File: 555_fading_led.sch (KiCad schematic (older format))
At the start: 15 parts, among them SW1 power, U1 TLC555, U2 TLC555

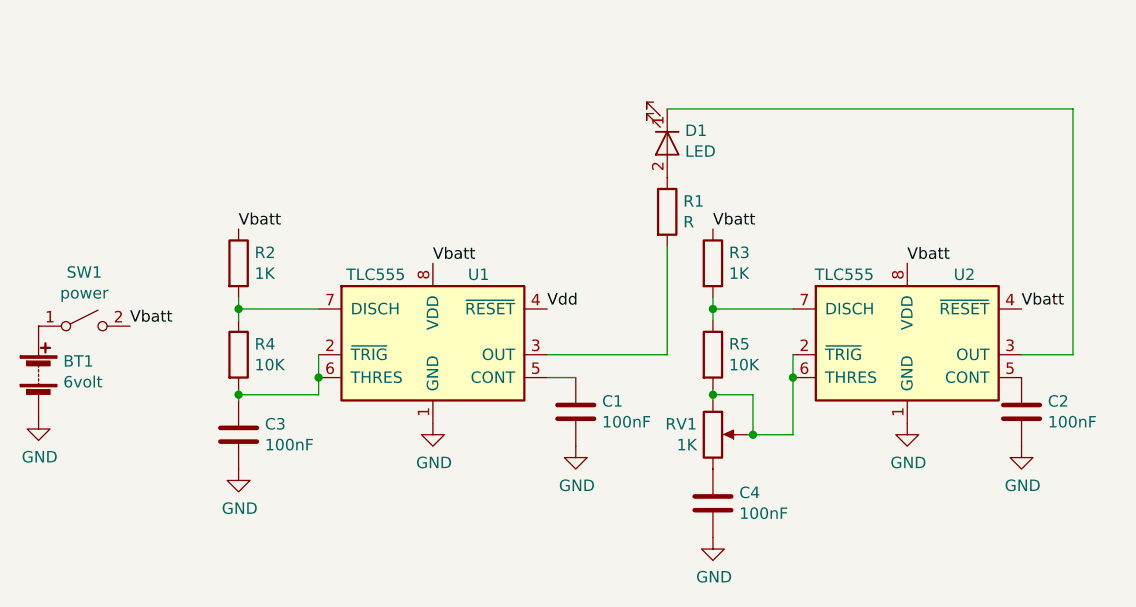
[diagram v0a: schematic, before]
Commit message: modification to schematic to add a second LED
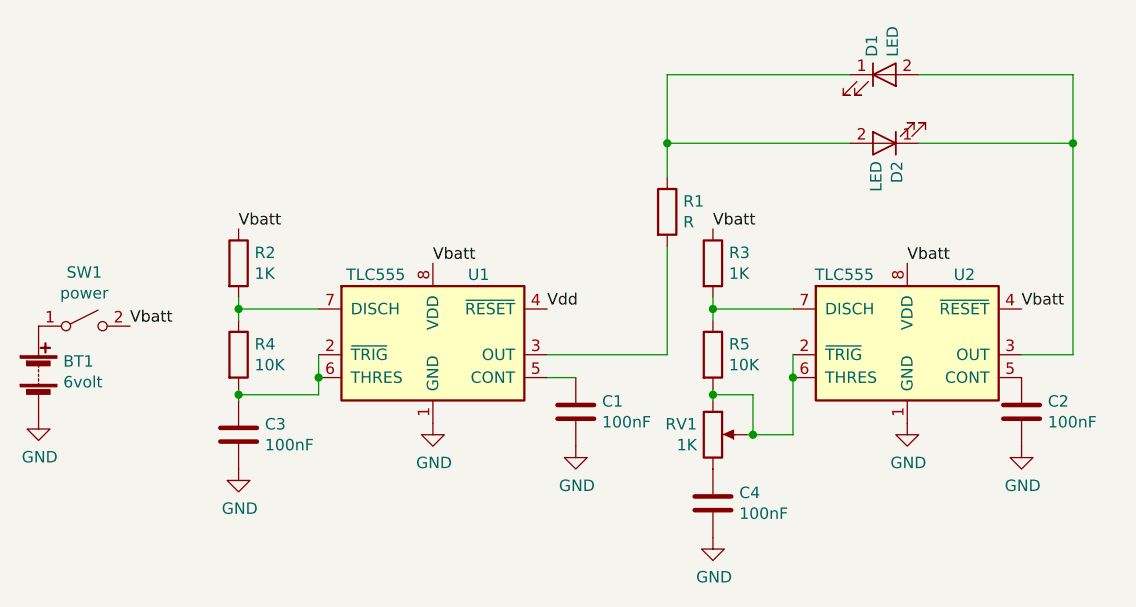
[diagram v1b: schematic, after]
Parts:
- added D1: LED, R, symbol device:LED
- renumbered D1 to D2
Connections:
- net at D2.1 (K), U2.3 (OUT): now also D1.2 (A)
- net at D2.2 (A), R1.1: now also D1.1 (K)
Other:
- moved on the sheet: D2
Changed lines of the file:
@@
 EESchema Schematic File Version 4
+LIBS:555_fading_led-cache
 EELAYER 26 0
 EELAYER END
@@
 $EndComp
 $Comp
-L device:LED D1
+L device:LED D2
 U 1 1 5C20033B
-P 5675 2375
-F 0 "D1" V 5620 2453 50  0000 L CNN
-F 1 "LED" V 5711 2453 50  0000 L CNN
-F 2 "R" H 5675 2375 50  0001 C CNN
-F 3 "" H 5675 2375 50  0001 C CNN
-	1    5675 2375
-	0    1    1    0
+P 6625 2375
+F 0 "D2" V 6570 2453 50  0000 L CNN
+F 1 "LED" V 6661 2453 50  0000 L CNN
+F 2 "R" H 6625 2375 50  0001 C CNN
+F 3 "" H 6625 2375 50  0001 C CNN
+	1    6625 2375
+	-1   0    0    1
 $EndComp
 $Comp
@@
 	5675 3300 5675 2825
 Wire Wire Line
-	5675 2225 7450 2225
-Wire Wire Line
-	7450 2225 7450 3300
-Wire Wire Line
 	7450 3300 7225 3300
 $Comp
@@
 	1    0    0    -1
 $EndComp
+$Comp
+L device:LED D1
+U 1 1 5C205CEF
+P 6625 2075
+F 0 "D1" V 6570 2153 50  0000 L CNN
+F 1 "LED" V 6661 2153 50  0000 L CNN
+F 2 "R" H 6625 2075 50  0001 C CNN
+F 3 "" H 6625 2075 50  0001 C CNN
+	1    6625 2075
+	1    0    0    -1
+$EndComp
+Wire Wire Line
+	5675 2525 5675 2375
+Wire Wire Line
+	5675 2375 6475 2375
+Wire Wire Line
+	6475 2075 5675 2075
+Wire Wire Line
+	5675 2075 5675 2375
+Connection ~ 5675 2375
+Wire Wire Line
+	6775 2375 7450 2375
+Connection ~ 7450 2375
+Wire Wire Line
+	7450 2375 7450 3300
+Wire Wire Line
+	7450 2075 6775 2075
+Wire Wire Line
+	7450 2075 7450 2375
 $EndSCHEMATC

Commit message: modification to schematic
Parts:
- R1: value R -> 100R
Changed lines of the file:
@@
 P 5675 2675
 F 0 "R1" H 5745 2721 50  0000 L CNN
-F 1 "R" H 5745 2630 50  0000 L CNN
+F 1 "100R" H 5425 2725 50  0000 L CNN
 F 2 "" V 5605 2675 50  0001 C CNN
 F 3 "" H 5675 2675 50  0001 C CNN

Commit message: added photos
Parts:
- added C1, C2: 100nF, symbol device:C
- added R2: 51R, symbol device:R
- C5: renamed from C3; value 100nF -> 220nF
- C6: renamed from C4; value 100nF -> 220nF
- R1: value 100R -> 51R
- R6: renamed from R5; value 10K -> 9K2
- RV1: value 1K -> 2K
- renumbered C1 to C3, C2 to C4, R2 to R3, R3 to R4, R4 to R5
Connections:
- net Vdd is gone; now on net Vbatt: U1.4 (~RESET)
- net GND: now also C1.2, C2.2
- net Vbatt: now also C1.1, C2.1
- net at D1.2 (A), D2.1 (K): now also R2.1; no longer U2.3 (OUT)
- new net: R2.2, U2.3 (OUT)
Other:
- moved on the sheet: BT1, SW1
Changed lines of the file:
@@
 U 1 1 5C20033B
 P 6625 2375
-F 0 "D2" V 6570 2453 50  0000 L CNN
-F 1 "LED" V 6661 2453 50  0000 L CNN
+F 0 "D2" H 6575 2250 50  0000 L CNN
+F 1 "LED" H 6575 2500 50  0000 L CNN
 F 2 "R" H 6625 2375 50  0001 C CNN
 F 3 "" H 6625 2375 50  0001 C CNN
@@
 P 5675 2675
 F 0 "R1" H 5745 2721 50  0000 L CNN
-F 1 "100R" H 5425 2725 50  0000 L CNN
+F 1 "51R" H 5425 2725 50  0000 L CNN
 F 2 "" V 5605 2675 50  0001 C CNN
 F 3 "" H 5675 2675 50  0001 C CNN
@@
 	7450 3300 7225 3300
 $Comp
-L device:R R4
+L device:R R5
 U 1 1 5C2004A4
 P 3800 3300
-F 0 "R4" H 3870 3346 50  0000 L CNN
+F 0 "R5" H 3870 3346 50  0000 L CNN
 F 1 "10K" H 3870 3255 50  0000 L CNN
 F 2 "" V 3730 3300 50  0001 C CNN
@@
 $EndComp
 $Comp
-L device:R R2
+L device:R R3
 U 1 1 5C2005C8
 P 3800 2900
-F 0 "R2" H 3870 2946 50  0000 L CNN
+F 0 "R3" H 3870 2946 50  0000 L CNN
 F 1 "1K" H 3870 2855 50  0000 L CNN
 F 2 "" V 3730 2900 50  0001 C CNN
@@
 	3800 3100 3800 3150
 $Comp
-L device:C C3
+L device:C C5
 U 1 1 5C200762
 P 3800 3650
-F 0 "C3" H 3915 3696 50  0000 L CNN
-F 1 "100nF" H 3915 3605 50  0000 L CNN
+F 0 "C5" H 3915 3696 50  0000 L CNN
+F 1 "220nF" H 3915 3605 50  0000 L CNN
 F 2 "" H 3838 3500 50  0001 C CNN
 F 3 "" H 3800 3650 50  0001 C CNN
@@
 Connection ~ 4150 3400
 $Comp
-L power:GND #PWR06
+L power:GND #PWR08
 U 1 1 5C2009B3
 P 3800 3800
-F 0 "#PWR06" H 3800 3550 50  0001 C CNN
+F 0 "#PWR08" H 3800 3550 50  0001 C CNN
 F 1 "GND" H 3805 3627 50  0000 C CNN
 F 2 "" H 3800 3800 50  0001 C CNN
@@
 $EndComp
 $Comp
-L power:GND #PWR02
+L power:GND #PWR04
 U 1 1 5C2009D3
 P 4650 3600
-F 0 "#PWR02" H 4650 3350 50  0001 C CNN
+F 0 "#PWR04" H 4650 3350 50  0001 C CNN
 F 1 "GND" H 4655 3427 50  0000 C CNN
 F 2 "" H 4650 3600 50  0001 C CNN
@@
 $EndComp
 $Comp
-L device:C C1
+L device:C C3
 U 1 1 5C2009FA
 P 5275 3550
-F 0 "C1" H 5390 3596 50  0000 L CNN
+F 0 "C3" H 5390 3596 50  0000 L CNN
 F 1 "100nF" H 5390 3505 50  0000 L CNN
 F 2 "" H 5313 3400 50  0001 C CNN
@@
 	5150 3400 5275 3400
 $Comp
-L power:GND #PWR04
+L power:GND #PWR06
 U 1 1 5C200B3E
 P 5275 3700
-F 0 "#PWR04" H 5275 3450 50  0001 C CNN
+F 0 "#PWR06" H 5275 3450 50  0001 C CNN
 F 1 "GND" H 5280 3527 50  0000 C CNN
 F 2 "" H 5275 3700 50  0001 C CNN
@@
 L device:Battery BT1
 U 1 1 5C200BC5
-P 2925 3375
-F 0 "BT1" H 3033 3421 50  0000 L CNN
-F 1 "6volt" H 3033 3330 50  0000 L CNN
-F 2 "" V 2925 3435 50  0001 C CNN
-F 3 "~" V 2925 3435 50  0001 C CNN
-	1    2925 3375
-	1    0    0    -1
-$EndComp
-$Comp
-L power:GND #PWR01
+P 3400 2950
+F 0 "BT1" H 3508 2996 50  0000 L CNN
+F 1 "6volt" H 3508 2905 50  0000 L CNN
+F 2 "" V 3400 3010 50  0001 C CNN
+F 3 "~" V 3400 3010 50  0001 C CNN
+	1    3400 2950
+	1    0    0    -1
+$EndComp
+$Comp
+L power:GND #PWR03
 U 1 1 5C200C21
-P 2925 3575
-F 0 "#PWR01" H 2925 3325 50  0001 C CNN
-F 1 "GND" H 2930 3402 50  0000 C CNN
-F 2 "" H 2925 3575 50  0001 C CNN
-F 3 "" H 2925 3575 50  0001 C CNN
-	1    2925 3575
-	1    0    0    -1
-$EndComp
-Text Label 3325 3175 0    50   ~ 0
-Vbatt
+P 3400 3150
+F 0 "#PWR03" H 3400 2900 50  0001 C CNN
+F 1 "GND" H 3405 2977 50  0000 C CNN
+F 2 "" H 3400 3150 50  0001 C CNN
+F 3 "" H 3400 3150 50  0001 C CNN
+	1    3400 3150
+	1    0    0    -1
+$EndComp
 Text Label 3800 2750 0    50   ~ 0
 Vbatt
@@
 Vbatt
 $Comp
-L device:C C2
+L device:C C4
 U 1 1 5C200D1F
 P 7225 3550
-F 0 "C2" H 7340 3596 50  0000 L CNN
+F 0 "C4" H 7340 3596 50  0000 L CNN
 F 1 "100nF" H 7340 3505 50  0000 L CNN
 F 2 "100nF" H 7263 3400 50  0001 C CNN
@@
 $EndComp
 $Comp
-L power:GND #PWR05
+L power:GND #PWR07
 U 1 1 5C200D26
 P 7225 3700
-F 0 "#PWR05" H 7225 3450 50  0001 C CNN
+F 0 "#PWR07" H 7225 3450 50  0001 C CNN
 F 1 "GND" H 7230 3527 50  0000 C CNN
 F 2 "" H 7225 3700 50  0001 C CNN
@@
 $EndComp
 $Comp
-L power:GND #PWR03
+L power:GND #PWR05
 U 1 1 5C200DEE
 P 6725 3600
-F 0 "#PWR03" H 6725 3350 50  0001 C CNN
+F 0 "#PWR05" H 6725 3350 50  0001 C CNN
 F 1 "GND" H 6730 3427 50  0000 C CNN
 F 2 "" H 6725 3600 50  0001 C CNN
@@
 Vbatt
 Text Label 5150 3100 0    50   ~ 0
-Vdd
-$Comp
-L device:R R5
+Vbatt
+$Comp
+L device:R R6
 U 1 1 5C200EF2
 P 5875 3300
-F 0 "R5" H 5945 3346 50  0000 L CNN
-F 1 "10K" H 5945 3255 50  0000 L CNN
+F 0 "R6" H 5945 3346 50  0000 L CNN
+F 1 "9K2" H 5945 3255 50  0000 L CNN
 F 2 "" V 5805 3300 50  0001 C CNN
 F 3 "" H 5875 3300 50  0001 C CNN
@@
 $EndComp
 $Comp
-L device:R R3
+L device:R R4
 U 1 1 5C200EF9
 P 5875 2900
-F 0 "R3" H 5945 2946 50  0000 L CNN
+F 0 "R4" H 5945 2946 50  0000 L CNN
 F 1 "1K" H 5945 2855 50  0000 L CNN
 F 2 "" V 5805 2900 50  0001 C CNN
@@
 	5875 3100 5875 3150
 $Comp
-L device:C C4
+L device:C C6
 U 1 1 5C200F04
 P 5875 3950
-F 0 "C4" H 5990 3996 50  0000 L CNN
-F 1 "100nF" H 5990 3905 50  0000 L CNN
+F 0 "C6" H 5990 3996 50  0000 L CNN
+F 1 "220nF" H 5990 3905 50  0000 L CNN
 F 2 "" H 5913 3800 50  0001 C CNN
 F 3 "" H 5875 3950 50  0001 C CNN
@@
 $EndComp
 $Comp
-L power:GND #PWR07
+L power:GND #PWR09
 U 1 1 5C200F0F
 P 5875 4100
-F 0 "#PWR07" H 5875 3850 50  0001 C CNN
+F 0 "#PWR09" H 5875 3850 50  0001 C CNN
 F 1 "GND" H 5880 3927 50  0000 C CNN
 F 2 "" H 5875 4100 50  0001 C CNN
@@
 P 5875 3650
 F 0 "RV1" H 5805 3696 50  0000 R CNN
-F 1 "1K" H 5805 3605 50  0000 R CNN
+F 1 "2K" H 5805 3605 50  0000 R CNN
 F 2 "" H 5875 3650 50  0001 C CNN
 F 3 "" H 5875 3650 50  0001 C CNN
@@
 L switches:SW_SPST SW1
 U 1 1 5C20222B
-P 3125 3175
-F 0 "SW1" H 3125 3410 50  0000 C CNN
-F 1 "power" H 3125 3319 50  0000 C CNN
-F 2 "" H 3125 3175 50  0001 C CNN
-F 3 "" H 3125 3175 50  0001 C CNN
-	1    3125 3175
-	1    0    0    -1
-$EndComp
+P 3600 2750
+F 0 "SW1" H 3600 2985 50  0000 C CNN
+F 1 "power" H 3600 2894 50  0000 C CNN
+F 2 "" H 3600 2750 50  0001 C CNN
+F 3 "" H 3600 2750 50  0001 C CNN
+	1    3600 2750
+	1    0    0    -1
+$EndComp
+Wire Wire Line
+	5675 2525 5675 2375
+Wire Wire Line
+	5675 2375 6475 2375
+Wire Wire Line
+	6775 2375 7450 2375
+$Comp
+L device:C C1
+U 1 1 5C214838
+P 4500 2500
+F 0 "C1" V 4650 2475 50  0000 L CNN
+F 1 "100nF" V 4350 2475 50  0000 L CNN
+F 2 "" H 4538 2350 50  0001 C CNN
+F 3 "" H 4500 2500 50  0001 C CNN
+	1    4500 2500
+	0    1    1    0
+$EndComp
+$Comp
+L power:GND #PWR01
+U 1 1 5C214BF4
+P 4350 2500
+F 0 "#PWR01" H 4350 2250 50  0001 C CNN
+F 1 "GND" H 4355 2327 50  0000 C CNN
+F 2 "" H 4350 2500 50  0001 C CNN
+F 3 "" H 4350 2500 50  0001 C CNN
+	1    4350 2500
+	0    1    1    0
+$EndComp
+Wire Wire Line
+	4650 2500 4650 2900
+$Comp
+L device:C C2
+U 1 1 5C215037
+P 6575 2700
+F 0 "C2" V 6725 2675 50  0000 L CNN
+F 1 "100nF" V 6525 2750 50  0000 L CNN
+F 2 "" H 6613 2550 50  0001 C CNN
+F 3 "" H 6575 2700 50  0001 C CNN
+	1    6575 2700
+	0    1    1    0
+$EndComp
+$Comp
+L power:GND #PWR02
+U 1 1 5C21503E
+P 6425 2700
+F 0 "#PWR02" H 6425 2450 50  0001 C CNN
+F 1 "GND" H 6430 2527 50  0000 C CNN
+F 2 "" H 6425 2700 50  0001 C CNN
+F 3 "" H 6425 2700 50  0001 C CNN
+	1    6425 2700
+	0    1    1    0
+$EndComp
+Wire Wire Line
+	6725 2700 6725 2900
 $Comp
 L device:LED D1
-U 1 1 5C205CEF
-P 6625 2075
-F 0 "D1" V 6570 2153 50  0000 L CNN
-F 1 "LED" V 6661 2153 50  0000 L CNN
-F 2 "R" H 6625 2075 50  0001 C CNN
-F 3 "" H 6625 2075 50  0001 C CNN
-	1    6625 2075
-	1    0    0    -1
-$EndComp
-Wire Wire Line
-	5675 2525 5675 2375
-Wire Wire Line
-	5675 2375 6475 2375
-Wire Wire Line
-	6475 2075 5675 2075
-Wire Wire Line
-	5675 2075 5675 2375
+U 1 1 5C21A1DE
+P 6625 2025
+F 0 "D1" H 6575 1900 50  0000 L CNN
+F 1 "LED" H 6575 2150 50  0000 L CNN
+F 2 "R" H 6625 2025 50  0001 C CNN
+F 3 "" H 6625 2025 50  0001 C CNN
+	1    6625 2025
+	1    0    0    -1
+$EndComp
+Wire Wire Line
+	6475 2025 5675 2025
+Wire Wire Line
+	5675 2025 5675 2375
 Connection ~ 5675 2375
 Wire Wire Line
-	6775 2375 7450 2375
+	6775 2025 7450 2025
+Wire Wire Line
+	7450 2025 7450 2375
+$Comp
+L device:R R2
+U 1 1 5C21AA8D
+P 7450 2675
+F 0 "R2" H 7520 2721 50  0000 L CNN
+F 1 "51R" H 7200 2725 50  0000 L CNN
+F 2 "" V 7380 2675 50  0001 C CNN
+F 3 "" H 7450 2675 50  0001 C CNN
+	1    7450 2675
+	1    0    0    -1
+$EndComp
+Wire Wire Line
+	7450 3300 7450 2825
+Wire Wire Line
+	7450 2525 7450 2375
 Connection ~ 7450 2375
-Wire Wire Line
-	7450 2375 7450 3300
-Wire Wire Line
-	7450 2075 6775 2075
-Wire Wire Line
-	7450 2075 7450 2375
 $EndSCHEMATC
